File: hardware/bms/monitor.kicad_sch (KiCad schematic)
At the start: 98 parts

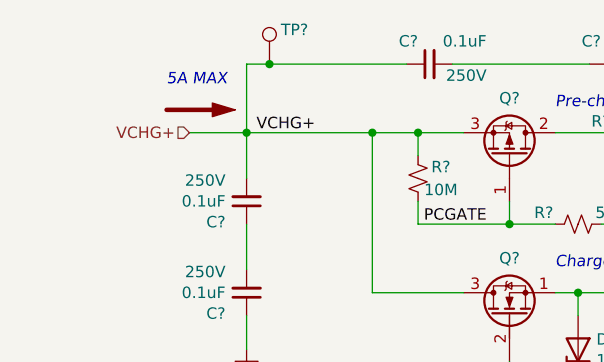
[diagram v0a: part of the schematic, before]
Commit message: Added charger and pack fuses directly to board
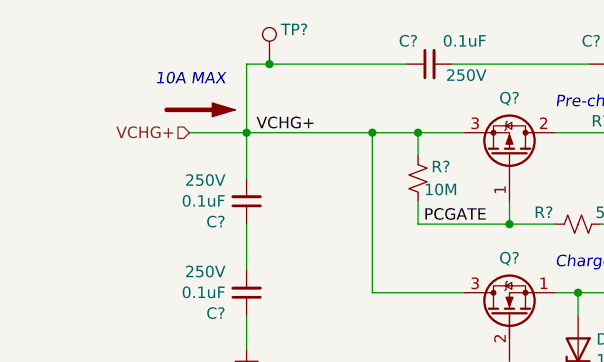
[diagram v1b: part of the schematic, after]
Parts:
- Q?: MFG PN BSC109N10NS3GATMA1 -> BSC034N10LS5ATMA1; RDS_ON 10.9m -> 3.4m
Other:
- note added: "10A MAX"
- note removed: "5A MAX"

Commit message: More charger sch progress
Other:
- note added: "Vishay Dale 2512 CSR. 12C/W, == 25C temp rise at nominal 45-50A load."
- note removed: "Vishay Dale 2512 CSR. 12C/W, means 25C temp rise at nominal 45-50A load."
- moved on the sheet: C?, TP?

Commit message: Made more progress on charger sch. Need to complete power stage next. Also added diode OR for MCU power conv input. Still deciding on converter selection
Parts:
- removed D?: D_Schottky, Diode_SMD:D_SOD-123, symbol Device:D_Schottky
- added D?: D_Schottky, Diode_SMD:D_SOD-123F, symbol Device:D_Schottky
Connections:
- net VBAT+: now also D?.2 (A)
- net at R?.1: now also D?.1 (K)

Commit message: Selected charger FETs, replaced other charger FETs to match. FETs rated for 40V since this is a 6S board (25.2V MAX). Also downsized the discharge FETs to be smaller and cheaper by selecting 40V FETs.
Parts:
- removed Q? (x2): Q_NMOS_GSD, Package_TO_SOT_SMD:Infineon_PG-HSOF-8-1, symbol Device:Q_NMOS_GSD
- removed Q?: Q_NMOS_SGD, bms:PG-TDSON-8, symbol Device:Q_NMOS_SGD
- added Q? (x2): IAUC120N04S6N006ATMA1, bms:PG-TDSON-8, symbol Device:Q_NMOS_SGD
- added Q?: BSZ018N04LS6ATMA1, bms:PG-TSDSON-8-26_INF, symbol Device:Q_NMOS_SGD
- Q? (x2): VDS (none) -> 100V
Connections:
- net CGATE: now also Q?.2 (G)
- net PACK+: now also Q?.1 (S), Q?.1 (S)
- net VBAT+: now also Q?.1 (S), Q?.3 (D), Q?.3 (D)
- net VCHG+: now also Q?.3 (D)
- net at R?.1: now also Q?.2 (G) (x2)
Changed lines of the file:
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@@
       (effects (font (size 1.27 1.27)) hide)
+    )
+    (property "VDS" "100V" (at 77.47 26.67 90)
+      (effects (font (size 1.27 1.27)))
     )
     (pin "1")
@@
       (effects (font (size 1.27 1.27)) hide)
     )
-    (pin "1")
-    (pin "2")
-    (pin "3")
-    (instances
-      (project "bms"
-        (path "/a4805e9d-b940-444e-a7cb-db4f4c53ed46/00000000-0000-0000-0000-00006523a805"
-          (reference "Q?") (unit 1)
-        )
-      )
-    )
-  )
-  (symbol (lib_id "Device:Q_NMOS_GSD") (at 204.47 49.53 90) (unit 1)
-    (in_bom yes) (on_board yes) (dnp no)
-    (property "Reference" "Q?" (at 204.47 43.1546 90)
-      (effects (font (size 1.27 1.27)))
-    )
-    (property "Value" "Q_NMOS_GSD" (at 204.47 43.1546 90)
-      (effects (font (size 1.27 1.27)) hide)
-    )
-    (property "Footprint" "Package_TO_SOT_SMD:Infineon_PG-HSOF-8-1" (at 201.93 44.45 0)
-      (effects (font (size 1.27 1.27)) hide)
-    )
-    (property "Datasheet" "~" (at 204.47 49.53 0)
-      (effects (font (size 1.27 1.27)) hide)
-    )
-    (property "MFG" "Infineon" (at 204.47 49.53 90)
-      (effects (font (size 1.27 1.27)) hide)
-    )
-    (property "MFG PN" "IAUT300N10S5N014ATMA1" (at 204.47 49.53 90)
-      (effects (font (size 1.27 1.27)) hide)
-    )
-    (property "RDS_ON" "1.4m" (at 204.47 49.53 90)
-      (effects (font (size 1.27 1.27)) hide)
-    )
-    (property "VDS" "100V" (at 204.47 49.53 90)
-      (effects (font (size 1.27 1.27)) hide)
-    )
-    (pin "1")
-    (pin "2")
-    (pin "3")
-    (instances
-      (project "bms"
-        (path "/a4805e9d-b940-444e-a7cb-db4f4c53ed46/00000000-0000-0000-0000-00006523a805"
-          (reference "Q?") (unit 1)
-        )
-      )
-    )
-  )
-  (symbol (lib_id "Device:Q_NMOS_GSD") (at 204.47 64.77 90) (unit 1)
-    (in_bom yes) (on_board yes) (dnp no)
-    (property "Reference" "Q?" (at 204.47 58.3946 90)
-      (effects (font (size 1.27 1.27)))
-    )
-    (property "Value" "Q_NMOS_GSD" (at 204.47 58.3946 90)
-      (effects (font (size 1.27 1.27)) hide)
-    )
-    (property "Footprint" "Package_TO_SOT_SMD:Infineon_PG-HSOF-8-1" (at 201.93 59.69 0)
-      (effects (font (size 1.27 1.27)) hide)
-    )
-    (property "Datasheet" "~" (at 204.47 64.77 0)
-      (effects (font (size 1.27 1.27)) hide)
-    )
-    (property "MFG" "Infineon" (at 204.47 64.77 90)
-      (effects (font (size 1.27 1.27)) hide)
-    )
-    (property "MFG PN" "IAUT300N10S5N014ATMA1" (at 204.47 64.77 90)
-      (effects (font (size 1.27 1.27)) hide)
-    )
-    (property "RDS_ON" "1.4m" (at 204.47 64.77 90)
-      (effects (font (size 1.27 1.27)) hide)
-    )
-    (property "VDS" "100V" (at 204.47 64.77 90)
-      (effects (font (size 1.27 1.27)) hide)
-    )
-    (pin "1")
-    (pin "2")
-    (pin "3")
-    (instances
-      (project "bms"
-        (path "/a4805e9d-b940-444e-a7cb-db4f4c53ed46/00000000-0000-0000-0000-00006523a805"
-          (reference "Q?") (unit 1)
-        )
-      )
-    )
-  )
-  (symbol (lib_id "Device:Q_NMOS_SGD") (at 82.55 49.53 90) (unit 1)
-    (in_bom yes) (on_board yes) (dnp no)
-    (property "Reference" "Q?" (at 82.55 43.1546 90)
-      (effects (font (size 1.27 1.27)))
-    )
-    (property "Value" "Q_NMOS_SGD" (at 83.693 44.3484 0)
-      (effects (font (size 1.27 1.27)) (justify left) hide)
-    )
-    (property "Footprint" "bms:PG-TDSON-8" (at 80.01 44.45 0)
-      (effects (font (size 1.27 1.27)) hide)
-    )
-    (property "Datasheet" "~" (at 82.55 49.53 0)
-      (effects (font (size 1.27 1.27)) hide)
-    )
-    (property "MFG" "Infineon" (at 82.55 49.53 90)
-      (effects (font (size 1.27 1.27)) hide)
-    )
-    (property "MFG PN" "BSC034N10LS5ATMA1" (at 82.55 49.53 90)
-      (effects (font (size 1.27 1.27)) hide)
-    )
-    (property "VDS" "100V" (at 82.55 49.53 90)
-      (effects (font (size 1.27 1.27)) hide)
-    )
-    (property "RDS_ON" "3.4m" (at 82.55 49.53 90)
-      (effects (font (size 1.27 1.27)) hide)
+    (property "VDS" "100V" (at 209.55 27.94 90)
+      (effects (font (size 1.27 1.27)))
     )
     (pin "1")
@@
     )
   )
+  (symbol (lib_id "Device:Q_NMOS_SGD") (at 204.47 49.53 90) (unit 1)
+    (in_bom yes) (on_board yes) (dnp no)
+    (property "Reference" "Q?" (at 204.47 43.18 90)
+      (effects (font (size 1.27 1.27)))
+    )
+    (property "Value" "IAUC120N04S6N006ATMA1" (at 205.74 43.18 0)
+      (effects (font (size 1.27 1.27)) (justify left) hide)
+    )
+    (property "Footprint" "bms:PG-TDSON-8" (at 201.93 44.45 0)
+      (effects (font (size 1.27 1.27)) hide)
+    )
+    (property "Datasheet" "https://www.infineon.com/dgdl/Infineon-IAUC120N04S6N006-DataSheet-v01_00-EN.pdf?fileId=5546d46275b79adb0175e120b4b310b3" (at 204.47 49.53 0)
+      (effects (font (size 1.27 1.27)) hide)
+    )
+    (property "MFG" "Infineon Technologies" (at 204.47 49.53 0)
+      (effects (font (size 1.27 1.27)) hide)
+    )
+    (property "MFG PN" "IAUC120N04S6N006ATMA1" (at 204.47 49.53 0)
+      (effects (font (size 1.27 1.27)) hide)
+    )
+    (property "VDS" "40V" (at 209.55 45.72 90)
+      (effects (font (size 1.27 1.27)))
+    )
+    (property "VGS" "20V" (at 204.47 49.53 0)
+      (effects (font (size 1.27 1.27)) hide)
+    )
+    (property "RDS_ON" "0.6m" (at 204.47 49.53 0)
+      (effects (font (size 1.27 1.27)) hide)
+    )
+    (property "QSW" "37.5nC" (at 204.47 49.53 0)
+      (effects (font (size 1.27 1.27)) hide)
+    )
+    (pin "1")
+    (pin "2")
+    (pin "3")
+    (instances
+      (project "bms"
+        (path "/a4805e9d-b940-444e-a7cb-db4f4c53ed46/00000000-0000-0000-0000-00006523ab32"
+          (reference "Q?") (unit 1)
+        )
+        (path "/a4805e9d-b940-444e-a7cb-db4f4c53ed46/00000000-0000-0000-0000-00006523a805"
+          (reference "Q?") (unit 1)
+        )
+      )
+    )
+  )
   (symbol (lib_id "Device:D_Schottky") (at 127 74.93 180) (unit 1)
     (in_bom yes) (on_board yes) (dnp no)
@@
         )
       )
+    )
+  )
+  (symbol (lib_id "Device:Q_NMOS_SGD") (at 204.47 64.77 90) (unit 1)
+    (in_bom yes) (on_board yes) (dnp no)
+    (property "Reference" "Q?" (at 204.47 58.42 90)
+      (effects (font (size 1.27 1.27)))
+    )
+    (property "Value" "IAUC120N04S6N006ATMA1" (at 205.74 58.42 0)
+      (effects (font (size 1.27 1.27)) (justify left) hide)
+    )
+    (property "Footprint" "bms:PG-TDSON-8" (at 201.93 59.69 0)
+      (effects (font (size 1.27 1.27)) hide)
+    )
+    (property "Datasheet" "https://www.infineon.com/dgdl/Infineon-IAUC120N04S6N006-DataSheet-v01_00-EN.pdf?fileId=5546d46275b79adb0175e120b4b310b3" (at 204.47 64.77 0)
+      (effects (font (size 1.27 1.27)) hide)
+    )
+    (property "MFG" "Infineon Technologies" (at 204.47 64.77 0)
+      (effects (font (size 1.27 1.27)) hide)
+    )
+    (property "MFG PN" "IAUC120N04S6N006ATMA1" (at 204.47 64.77 0)
+      (effects (font (size 1.27 1.27)) hide)
+    )
+    (property "VDS" "40V" (at 209.55 60.96 90)
+      (effects (font (size 1.27 1.27)))
+    )
+    (property "VGS" "20V" (at 204.47 64.77 0)
+      (effects (font (size 1.27 1.27)) hide)
+    )
+    (property "RDS_ON" "0.6m" (at 204.47 64.77 0)
+      (effects (font (size 1.27 1.27)) hide)
+    )
+    (property "QSW" "37.5nC" (at 204.47 64.77 0)
+      (effects (font (size 1.27 1.27)) hide)
+    )
+    (pin "1")
+    (pin "2")
+    (pin "3")
+    (instances
+      (project "bms"
+        (path "/a4805e9d-b940-444e-a7cb-db4f4c53ed46/00000000-0000-0000-0000-00006523ab32"
+          (reference "Q?") (unit 1)
+        )
+        (path "/a4805e9d-b940-444e-a7cb-db4f4c53ed46/00000000-0000-0000-0000-00006523a805"
+          (reference "Q?") (unit 1)
+        )
+      )
+    )
+  )
+  (symbol (lib_id "Device:Q_NMOS_SGD") (at 82.55 49.53 90) (unit 1)
+    (in_bom yes) (on_board yes) (dnp no)
+    (property "Reference" "Q?" (at 82.55 43.18 90)
+      (effects (font (size 1.27 1.27)))
+    )
+    (property "Value" "BSZ018N04LS6ATMA1" (at 83.82 43.18 0)
+      (effects (font (size 1.27 1.27)) (justify left) hide)
+    )
+    (property "Footprint" "bms:PG-TSDSON-8-26_INF" (at 80.01 44.45 0)
+      (effects (font (size 1.27 1.27)) hide)
+    )
+    (property "Datasheet" "https://www.infineon.com/dgdl/Infineon-BSZ018N04LS6-DataSheet-v02_01-EN.pdf?fileId=5546d46269e1c0190169e2e8e05601f7" (at 82.55 49.53 0)
+      (effects (font (size 1.27 1.27)) hide)
+    )
+    (property "MFG" "Infineon Technologies" (at 82.55 49.53 0)
+      (effects (font (size 1.27 1.27)) hide)
+    )
+    (property "MFG PN" "BSZ018N04LS6ATMA1" (at 82.55 49.53 0)
+      (effects (font (size 1.27 1.27)) hide)
+    )
+    (property "VDS" "40V" (at 78.74 44.45 90)
+      (effects (font (size 1.27 1.27)))
+    )
+    (property "VGS" "20V" (at 82.55 49.53 0)
+      (effects (font (size 1.27 1.27)) hide)
+    )
+    (property "RDS_ON" "1.8m" (at 82.55 49.53 0)
+      (effects (font (size 1.27 1.27)) hide)
+    )
+    (property "QSW" "6nC" (at 82.55 49.53 0)
+      (effects (font (size 1.27 1.27)) hide)
+    )
+    (pin "1")
+    (pin "2")
+    (pin "3")
+    (instances
+      (project "bms"
+        (path "/a4805e9d-b940-444e-a7cb-db4f4c53ed46/00000000-0000-0000-0000-00006523ab32"
+          (reference "Q?") (unit 1)
+        )
+        (path "/a4805e9d-b940-444e-a7cb-db4f4c53ed46/00000000-0000-0000-0000-00006523a805"
+          (reference "Q?") (unit 1)
+        )
+      )

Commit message: Charger schematic complete! Only MCU left.
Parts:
- added R?: 10k, Resistor_SMD:R_0603_1608Metric, symbol Device:R_Small_US
- added TP? (x15): TestPoint, TestPoint:TestPoint_Pad_D1.0mm, symbol Connector:TestPoint
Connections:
- net BMS_WAKE: now also R?.1, TP?.1
- net GND: now also TP?.1, TP?.1, TP?.1, TP?.1
- net LD: now also TP?.1
- net PACK: now also TP?.1
- net THERM_1: now also TP?.1
- net THERM_2: now also TP?.1
- net THERM_3: now also TP?.1
- net THERM_4: now also TP?.1
- net THERM_5: now also TP?.1
- net THERM_6: now also TP?.1
- net THERM_7: now also TP?.1
- net THERM_8: now also TP?.1
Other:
- note added: "Adding pulldown BJT to ensure wakeup during charge"
- note added: "Possible alternative with lower RTH: TLR3APDTE1L00F75"
- moved on the sheet: C?

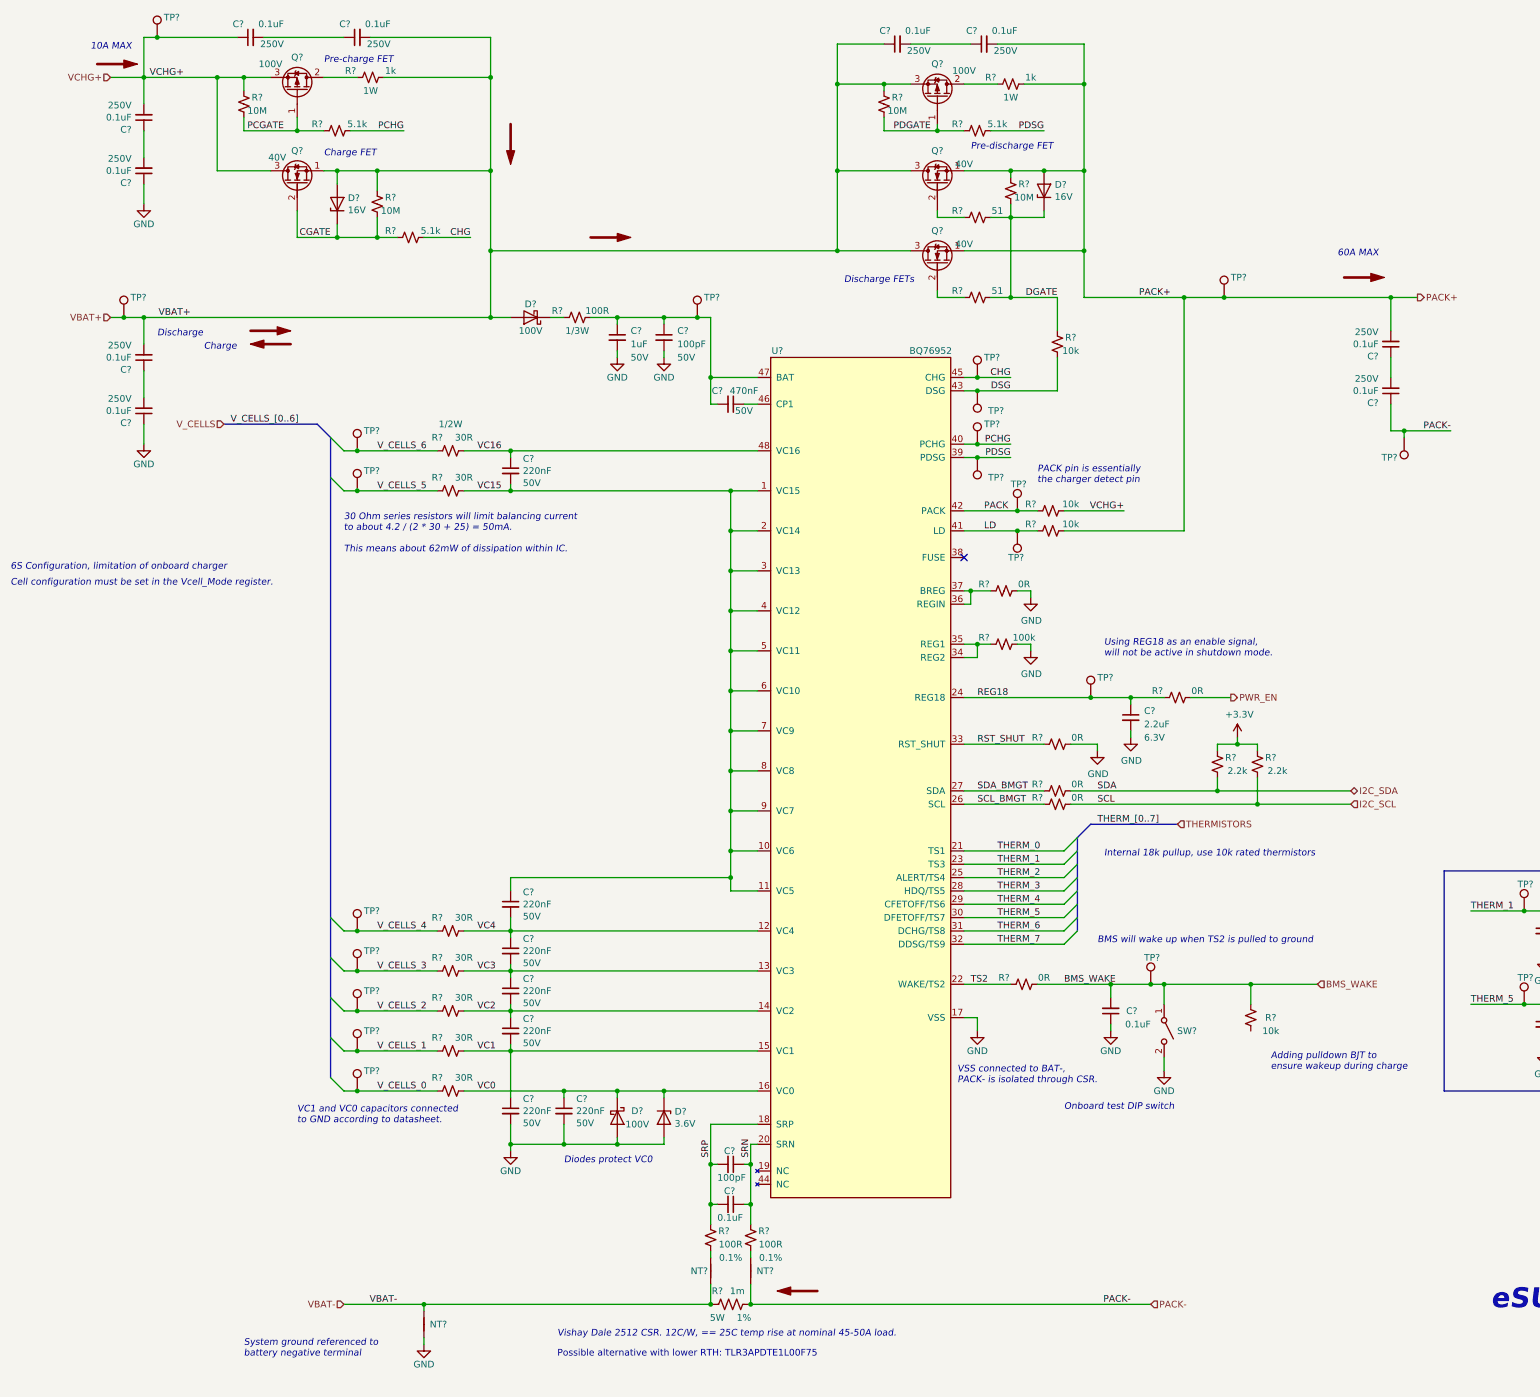
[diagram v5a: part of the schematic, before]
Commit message: Added BJT to enable BMS/MCU when charger input voltage present
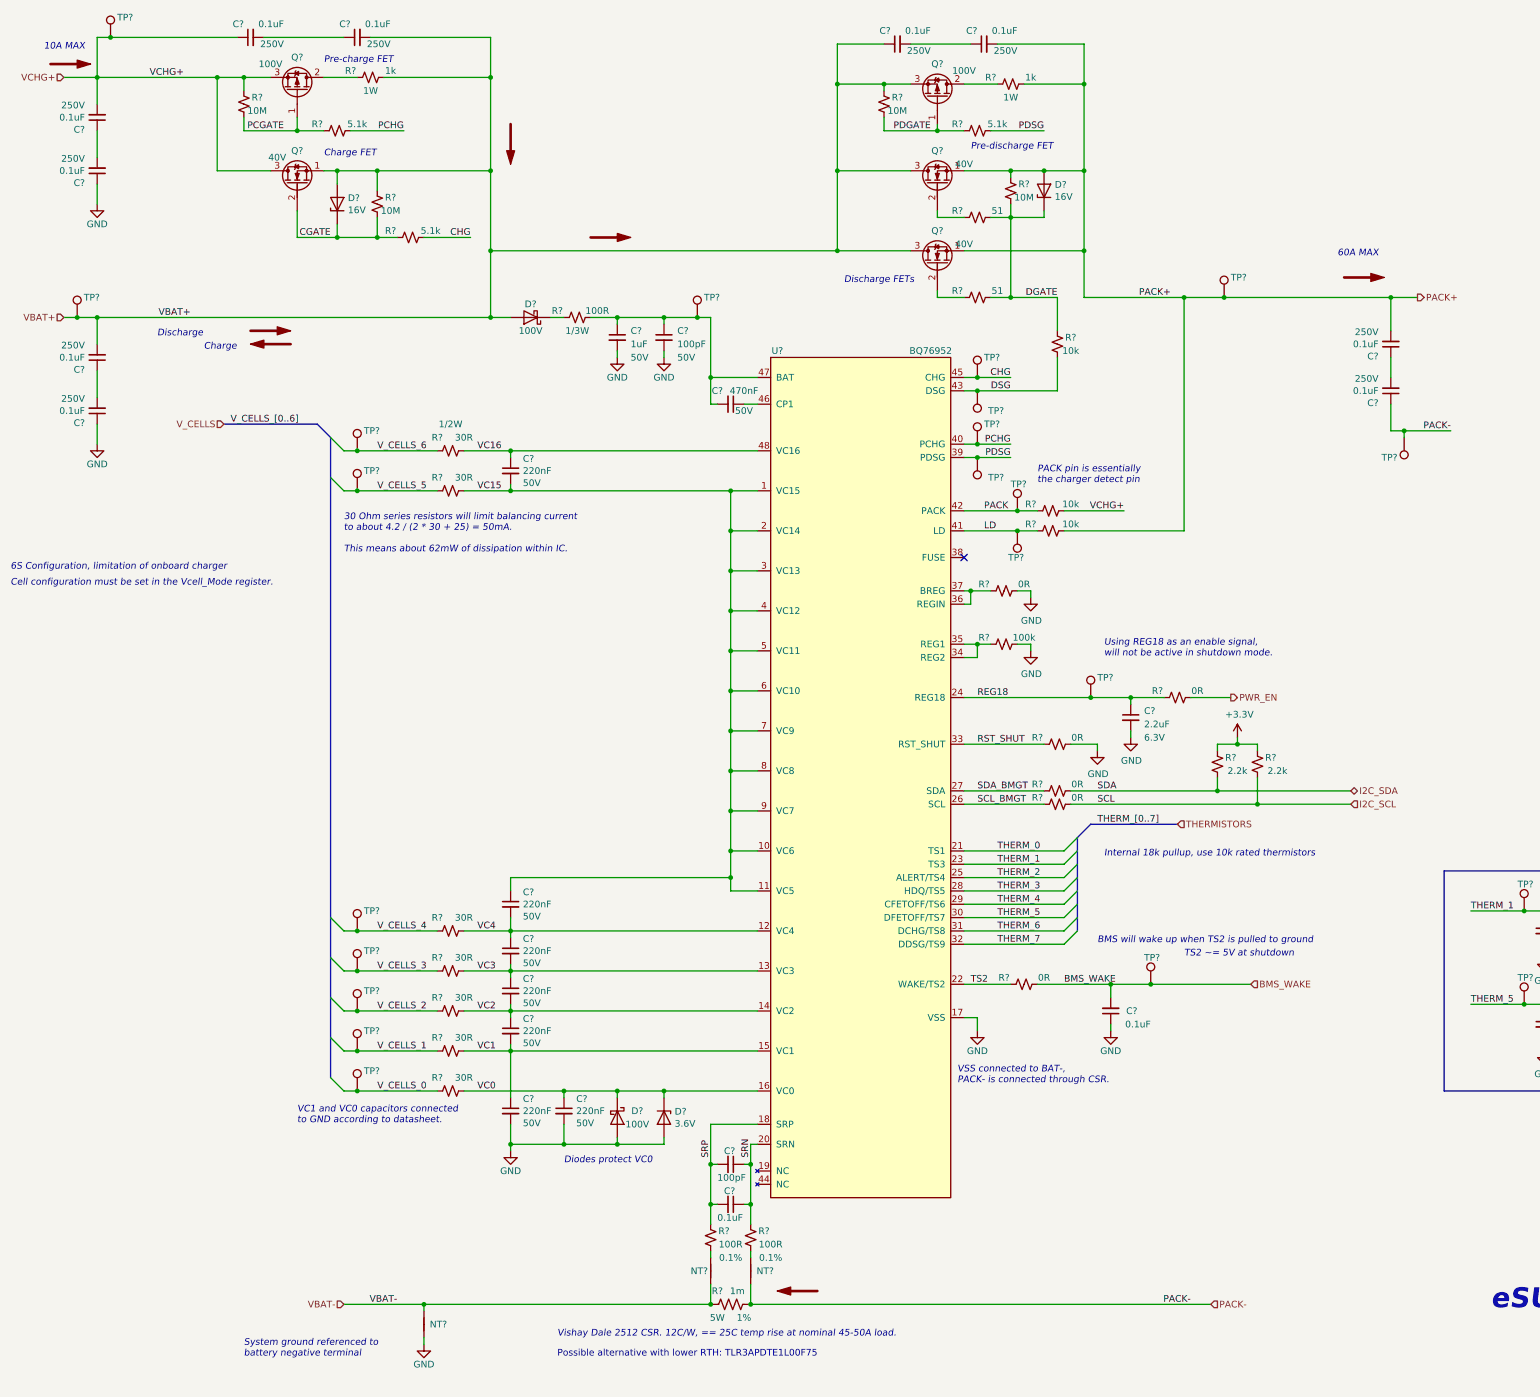
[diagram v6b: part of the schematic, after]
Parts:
- removed R?: 10k, Resistor_SMD:R_0603_1608Metric, symbol Device:R_Small_US
- removed SW?: SW_SPST, bms:SW_DS04-254-2-01BK-SMT-TR, symbol Switch:SW_SPST
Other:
- note added: "TS2 ~= 5V at shutdown"
- note added: "VSS connected to BAT-, PACK- is connected through CSR."
- note removed: "Adding pulldown BJT to ensure wakeup during charge"
- note removed: "Onboard test DIP switch"
- note removed: "VSS connected to BAT-, PACK- is isolated through CSR."
- moved on the sheet: C?, TP?
